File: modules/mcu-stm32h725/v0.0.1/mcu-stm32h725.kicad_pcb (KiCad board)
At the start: 4 copper layers, 68.6 x 18 mm, 37 parts, among them J1 USB-C, J2 Side A, J3 Side B, U1 USB6B1RL, U2 TLV62569DBVR, U3 STM32H725RGV3, U4 TPS2116DRLR, Y1 25MHz

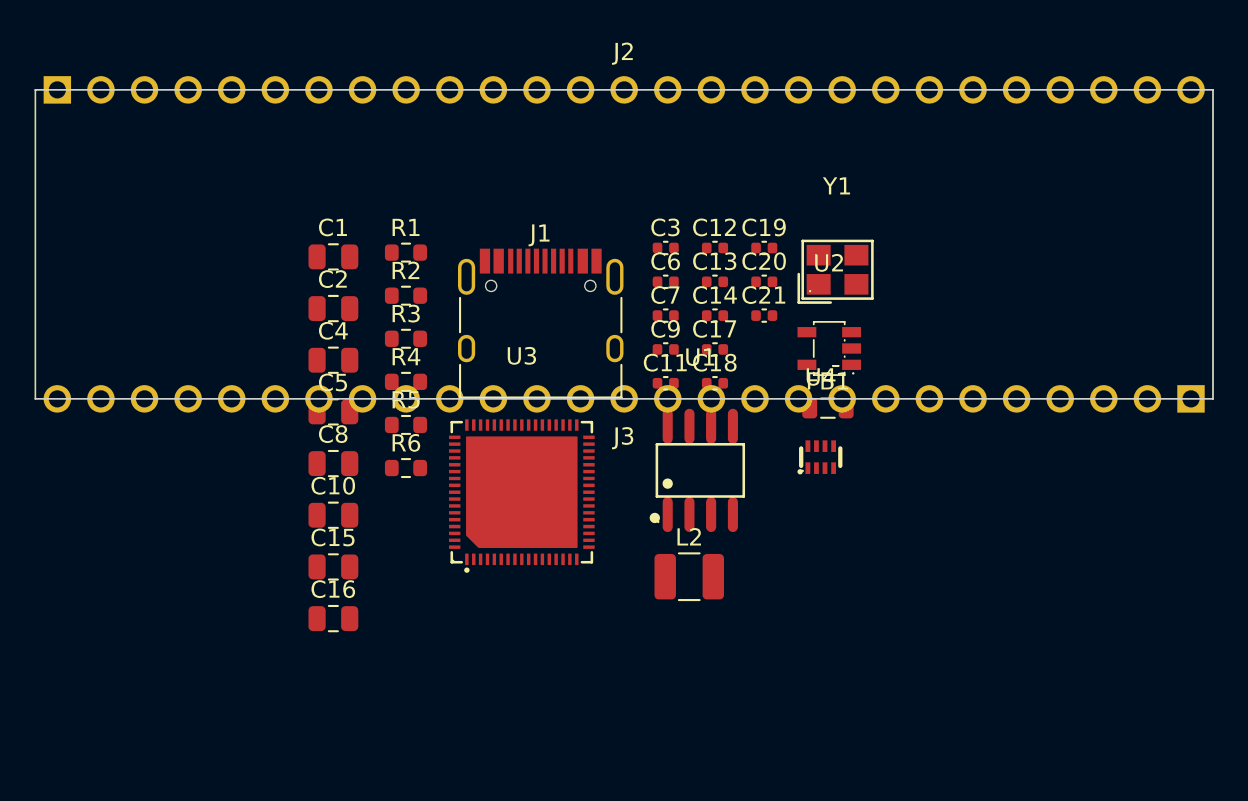
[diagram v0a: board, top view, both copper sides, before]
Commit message: Lay out mcu-stm32h725 PCB: centered placement + 4-layer planes + optimal pin map
All 38 footprints placed (MCU centered for balanced GPIO fan-out; power block by USB-C; decoupling ringing the MCU; bulk caps right). GND plane (In1.Cu) + +3V3 plane (In2.Cu) zones added + filled. Castellation pads marked pad_prop_castellated in board + library (clears edge-clearance DRC). Schematic fixes: L1 footprint L_1210_3225Metric; USB-C symbol -> USB_C_Receptacle_USB2.0_16P to match the 16-pad footprint; J1 instance annotation repaired. Castellation pin map is crossing-free per edge and optimal for the centered MCU (~656mm ratsnest). DRC: 0 electrical violations (only unrouted nets + cosmetic silk/fill remain). Routing pending.

Co-Authored-By: Claude Opus 4.8 <noreply@anthropic.com>
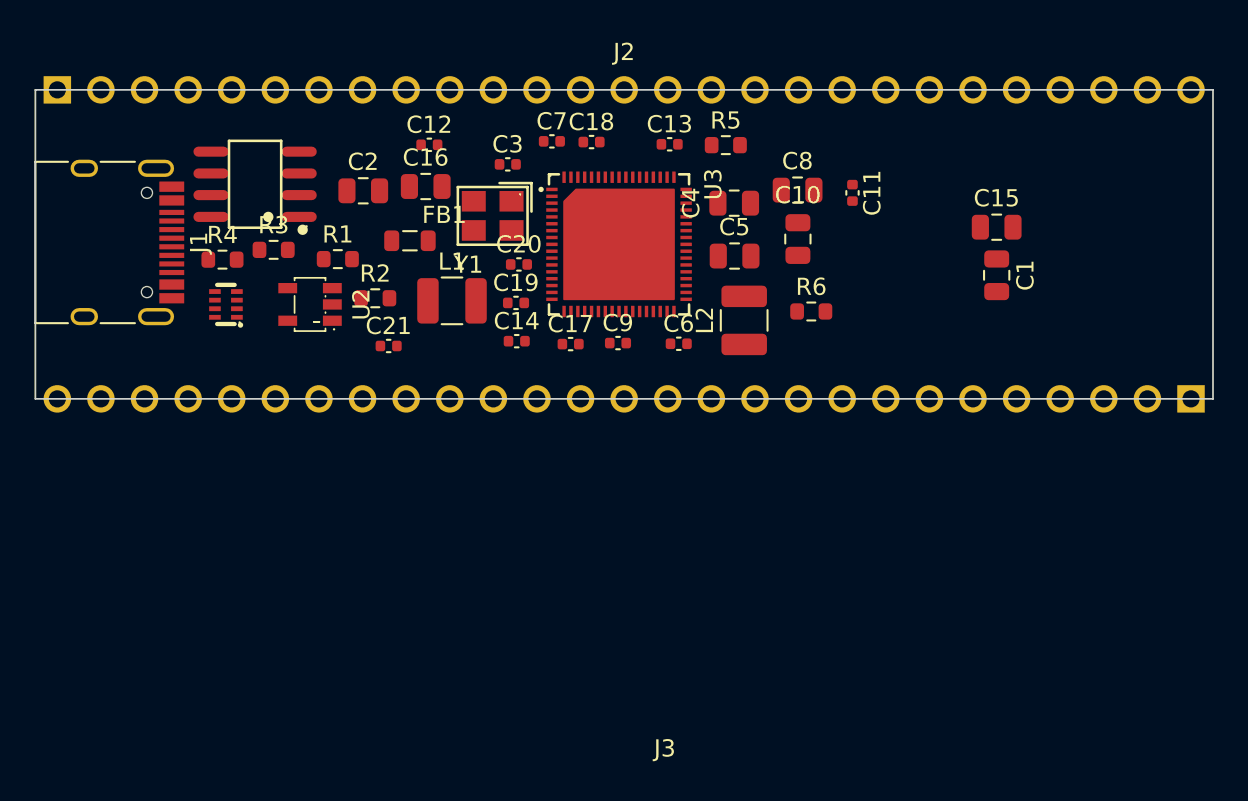
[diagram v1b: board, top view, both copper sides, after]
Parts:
- added L1: 2.2uH, Inductor_SMD:L_1210_3225Metric, F.Cu at (124.3, 152.3)
- moved C15 43.4 mm to (156.0, 148.0)
- moved C1 38.7 mm to (156.0, 150.8), turned to -90 degrees
- moved U4 35.8 mm to (111.1, 152.5), turned to 90 degrees
- moved C10 31.5 mm to (144.4, 148.7), turned to 90 degrees
- moved C8 31.4 mm to (144.4, 145.8)
- moved U1 30.8 mm to (112.8, 145.5), turned to 90 degrees
- moved U2 30.4 mm to (116.0, 152.5)
- moved FB1 26.2 mm to (121.8, 148.8), turned to 180 degrees
- moved J1 26.1 mm to (103.9, 148.9), turned to -90 degrees
- moved C16 25.7 mm to (122.7, 145.6)
- moved R6 25.3 mm to (145.2, 152.9)
- moved C4 25.1 mm to (140.7, 146.6), turned to 180 degrees
- moved C5 25.1 mm to (140.7, 149.7)
- moved R5 24.8 mm to (140.2, 143.2)
- moved C21 22.0 mm to (120.6, 154.9)
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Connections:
- J2 pad 10: /PA7 -> /PB4
- J2 pad 13: /PA8 -> /PB3
- J2 pad 14: /PA9 -> /PD2
- J2 pad 15: /PA10 -> /PC12
- J2 pad 20: /PA15 -> /PC11
- J2 pad 23: /PC0 -> /PC10
- J2 pad 24: /PC1 -> /PA15
- J2 pad 25: /PC4 -> /PA10
- J2 pad 26: /PC5 -> /PA9
- J2 pad 3: /PA0 -> /PC14
- J2 pad 4: /PA1 -> /PC15
- J2 pad 5: /PA2 -> /PB9
- J2 pad 6: /PA3 -> /PB8
- J2 pad 7: /PA4 -> /PB7
- J2 pad 8: /PA5 -> /PB6
- J2 pad 9: /PA6 -> /PB5
- J3 pad 10: /PB7 -> /PA8
- J3 pad 11: /PB8 -> /PB10
- J3 pad 12: /PB9 -> /PB2
- J3 pad 13: /PB10 -> /PB1
- J3 pad 15: /PB12 -> /PB0
- J3 pad 16: /PB13 -> /PC5
- J3 pad 17: /PB14 -> /PC4
- J3 pad 18: /PB15 -> /PA7
- J3 pad 19: /PC6 -> /PA6
- J3 pad 20: /PC7 -> /PA5
- J3 pad 21: /PC9 -> /PA4
- J3 pad 22: /PC10 -> /PA3
- J3 pad 23: /PC11 -> /PA2
- J3 pad 24: /PC12 -> /PA1
- J3 pad 25: /PC14 -> /PA0
- J3 pad 26: /PC15 -> /PC1
- J3 pad 27: /PD2 -> /PC0
- J3 pad 3: /PB0 -> /PB12
- J3 pad 4: /PB1 -> /PB13
- J3 pad 5: /PB2 -> /PB14
- J3 pad 6: /PB3 -> /PB15
- J3 pad 7: /PB4 -> /PC6
- J3 pad 8: /PB5 -> /PC7
- J3 pad 9: /PB6 -> /PC9
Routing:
- added copper zone on In2.Cu, net +3V3
- added copper zone on In1.Cu, net GND

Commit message: WIP: hand placement of mcu-stm32h725 (tight, pre-fan-out)
User's hand-arranged layout — good relative placement, tightly squished with sub-mm overlaps to be fanned out next. Tighten .bak* gitignore to catch backup variants.

Co-Authored-By: Claude Opus 4.8 <noreply@anthropic.com>
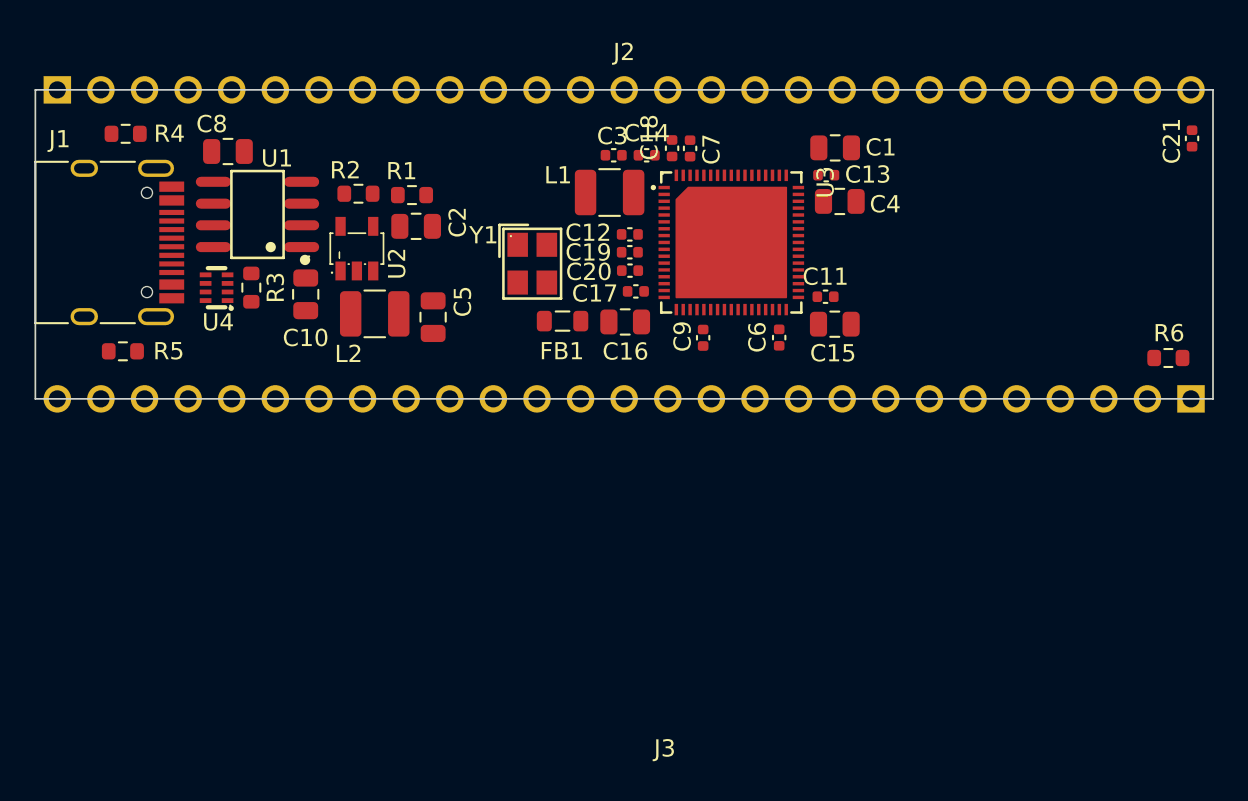
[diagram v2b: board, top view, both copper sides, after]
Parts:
- moved C21 48.3 mm to (167.4, 142.8), turned to -90 degrees
- moved R5 37.1 mm to (105.1, 155.2)
- moved C8 33.3 mm to (111.2, 143.6)
- moved C10 28.9 mm to (115.8, 151.9), turned to -90 degrees
- moved L2 21.5 mm to (119.8, 153.1), turned to 0 degrees
- moved R6 21.0 mm to (166.0, 155.6), turned to 180 degrees
- moved C5 17.9 mm to (123.2, 153.2), turned to 90 degrees
- moved C16 14.0 mm to (134.4, 153.5)
- moved C14 13.2 mm to (135.6, 143.8), turned to 180 degrees
- moved C12 12.8 mm to (134.6, 148.4), turned to 180 degrees
- moved C1 12.0 mm to (146.6, 143.4), turned to 0 degrees
- moved L1 11.1 mm to (133.4, 146.0)
- moved C15 11.0 mm to (146.6, 153.7)
- moved FB1 10.0 mm to (130.7, 153.5), turned to 0 degrees
- moved C13 9.30 mm to (146.1, 145.0)
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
